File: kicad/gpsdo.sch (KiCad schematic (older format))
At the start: 32 parts, among them J1 Conn_Coaxial, J2 Conn_01x04_Male, J3 Conn_01x04_Male, J4 Conn_01x04_Male, J5 Conn_01x04_Male, J6 Conn_01x04_Male, U1 MSP430F5171IDA, U11 47L64, U2 MAX-8Q, U3 549CAAC000111BBG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

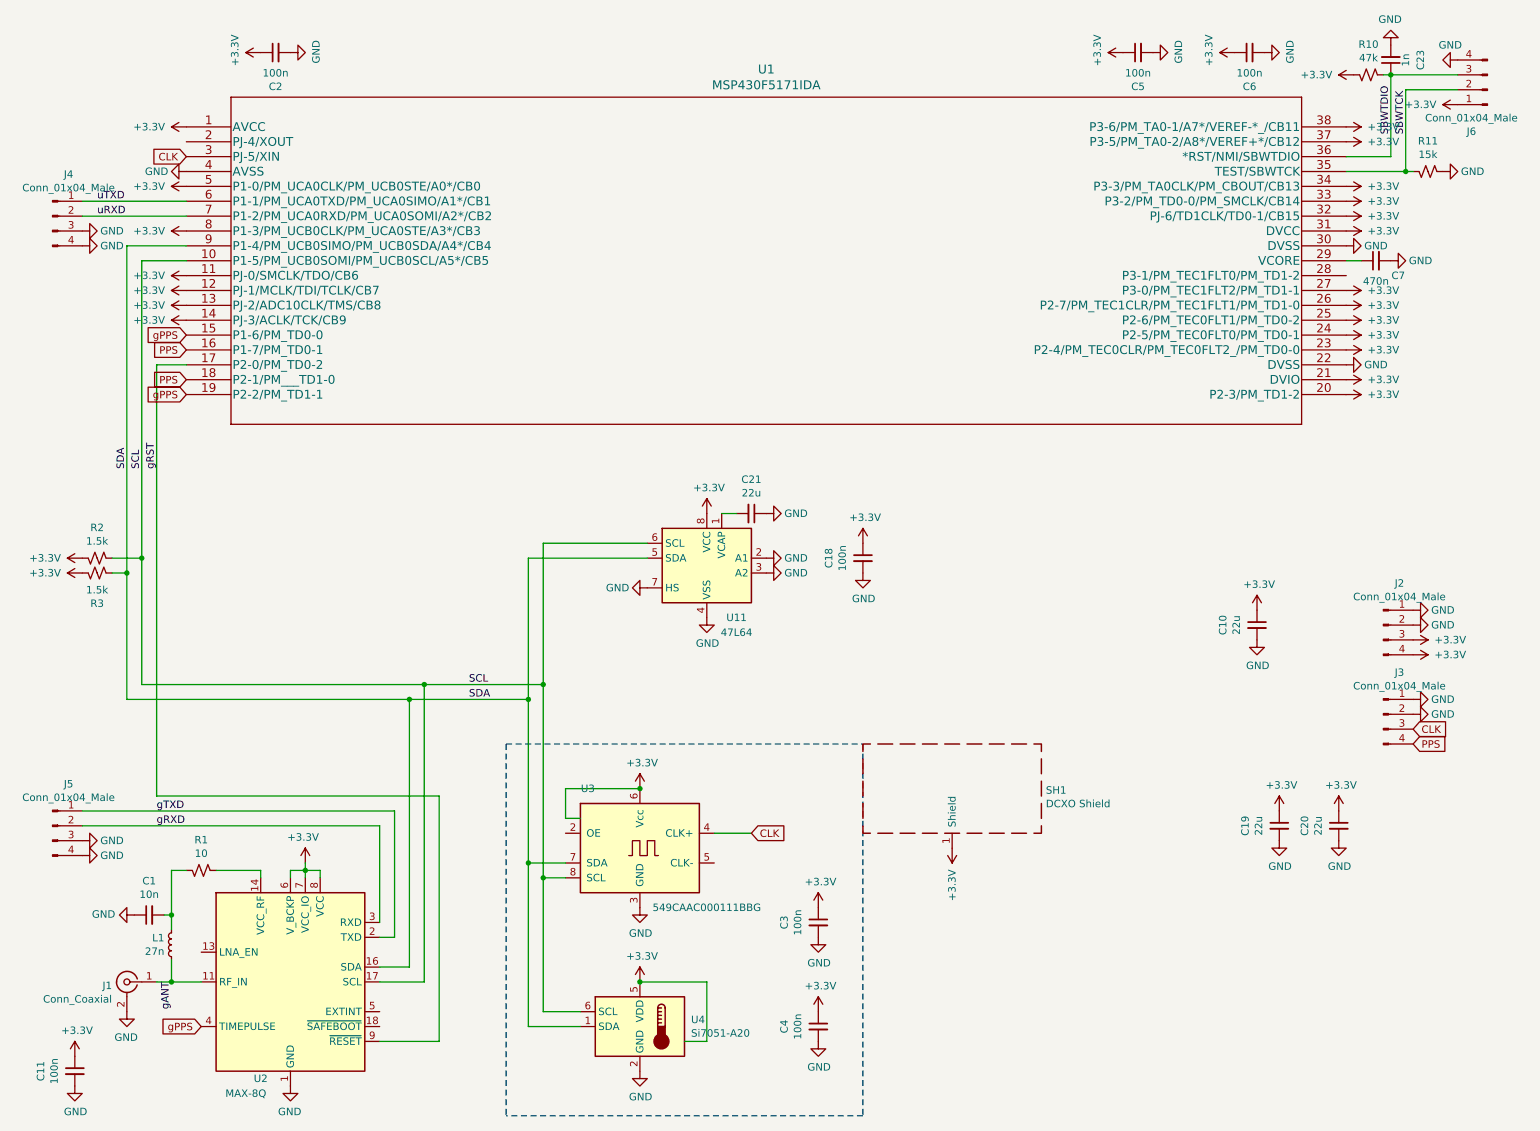
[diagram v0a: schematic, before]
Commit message: change Si549 to Si544
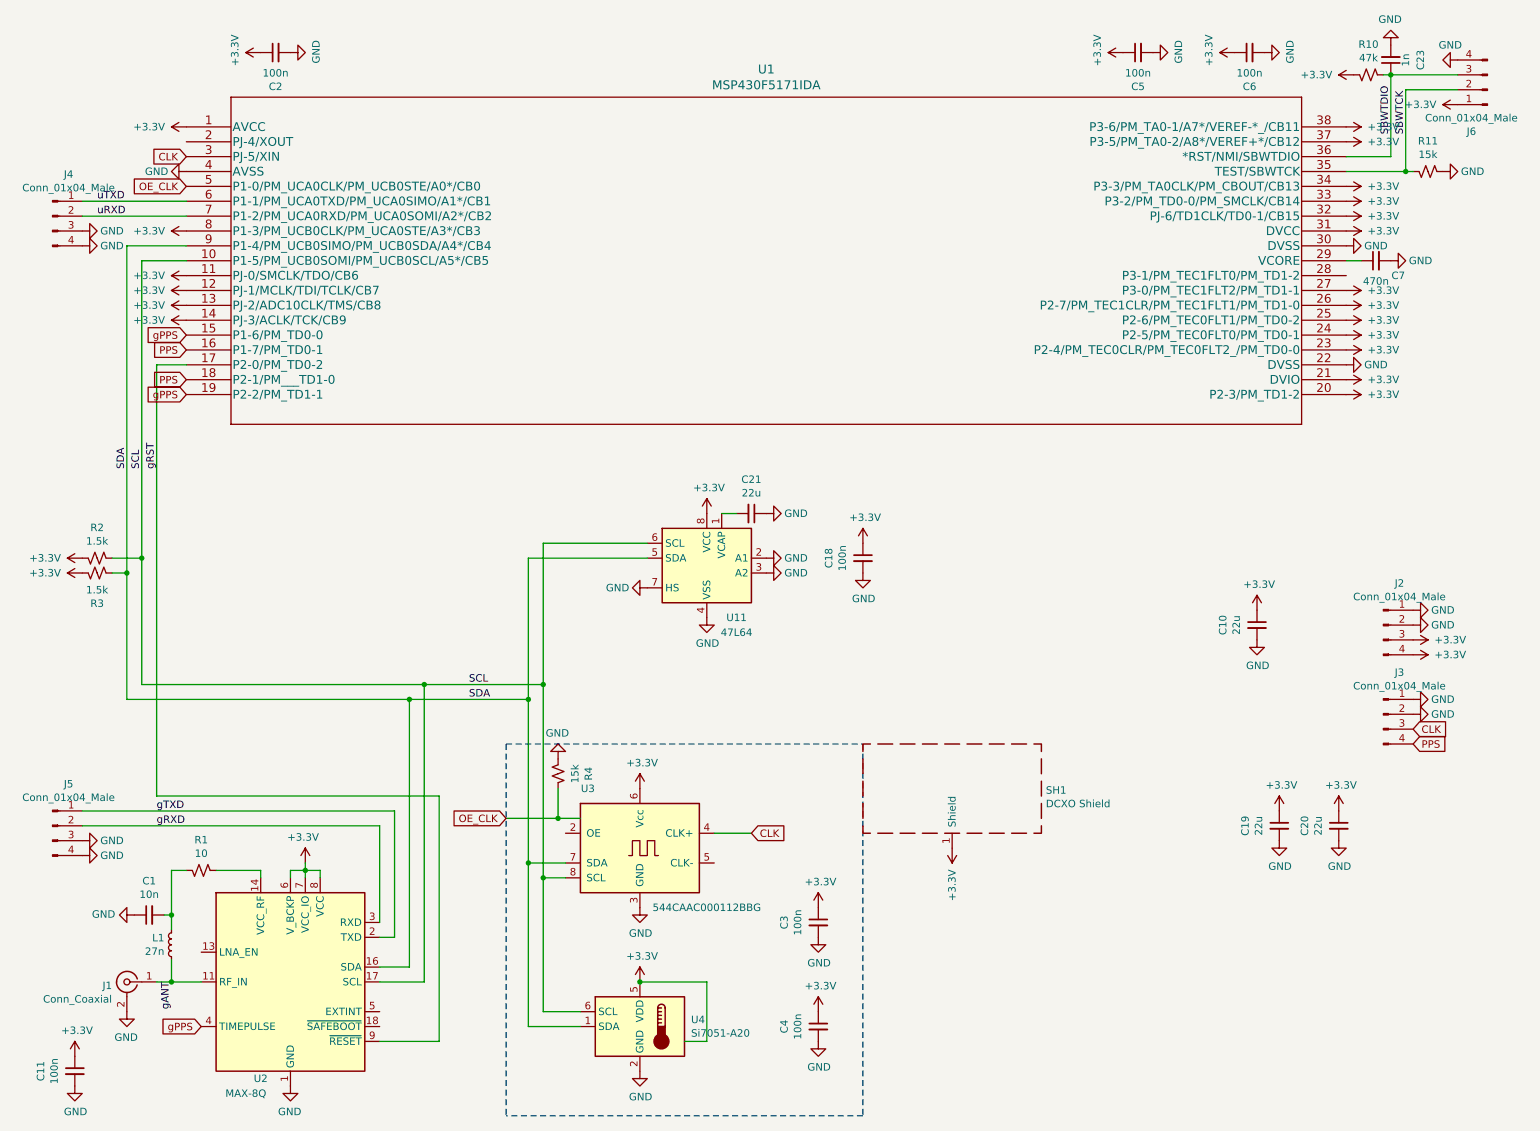
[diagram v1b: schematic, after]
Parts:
- added R4: 15k, Resistor_SMD:R_0603_1608Metric, symbol Device:R_Small_US
- U3: value 549CAAC000111BBG -> 544CAAC000112BBG
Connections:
- net +3V3: no longer U1.5 (P1-0/PM_UCA0CLK/PM_UCB0STE/A0*/CB0), U3.1 (NC)
- net GND: now also R4.1
- new net OE_CLK: R4.2, U1.5 (P1-0/PM_UCA0CLK/PM_UCB0STE/A0*/CB0), U3.1 (NC)
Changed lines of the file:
@@
 P 4650 6050
 F 0 "U3" H 4300 6450 50  0000 C CNN
-F 1 "549CAAC000111BBG" H 5100 5650 50  0000 C CNN
+F 1 "544CAAC000112BBG" H 5100 5650 50  0000 C CNN
 F 2 "Oscillator:Oscillator_SMD_SI570_SI571_Standard" H 4650 5750 50  0001 C CNN
 F 3 "http://www.silabs.com/Support%20Documents/TechnicalDocs/si570.pdf" H 4250 6750 50  0001 C CNN
@@
 	5100 6950 4650 6950
 Connection ~ 4650 6950
-Wire Wire Line
-	4250 5850 4150 5850
-Wire Wire Line
-	4150 5850 4150 5650
-Wire Wire Line
-	4150 5650 4650 5650
-Connection ~ 4650 5650
 $Comp
 L power:+3.3V #PWR0103
@@
 	0    -1   -1   0
 $EndComp
-$Comp
-L power:+3.3V #PWR0121
-U 1 1 611DA46C
-P 1600 1600
-F 0 "#PWR0121" H 1600 1450 50  0001 C CNN
-F 1 "+3.3V" V 1600 1850 50  0000 C CNN
-F 2 "" H 1600 1600 50  0001 C CNN
-F 3 "" H 1600 1600 50  0001 C CNN
-	1    1600 1600
-	0    -1   -1   0
-$EndComp
 Wire Wire Line
 	1400 5700 1400 2800
@@
 	0    1    1    0
 $EndComp
+Text GLabel 3750 5850 0    50   Input ~ 0
+OE_CLK
+Text GLabel 1600 1600 0    50   Input ~ 0
+OE_CLK
+Wire Wire Line
+	3750 5850 4100 5850
+$Comp
+L Device:R_Small_US R4
+U 1 1 610EB04B
+P 4100 5550
+F 0 "R4" V 3895 5550 50  0000 C CNN
+F 1 "15k" V 3986 5550 50  0000 C CNN
+F 2 "Resistor_SMD:R_0603_1608Metric" H 4100 5550 50  0001 C CNN
+F 3 "~" H 4100 5550 50  0001 C CNN
+	1    4100 5550
+	-1   0    0    -1
+$EndComp
+$Comp
+L power:GND #PWR0121
+U 1 1 610EB8DD
+P 4100 5450
+F 0 "#PWR0121" H 4100 5200 50  0001 C CNN
+F 1 "GND" H 4105 5277 50  0000 C CNN
+F 2 "" H 4100 5450 50  0001 C CNN
+F 3 "" H 4100 5450 50  0001 C CNN
+	1    4100 5450
+	-1   0    0    1
+$EndComp
+Wire Wire Line
+	4100 5650 4100 5850
+Connection ~ 4100 5850
+Wire Wire Line
+	4100 5850 4250 5850
 $EndSCHEMATC
